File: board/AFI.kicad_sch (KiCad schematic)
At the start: 2 parts, among them J3 2002411212

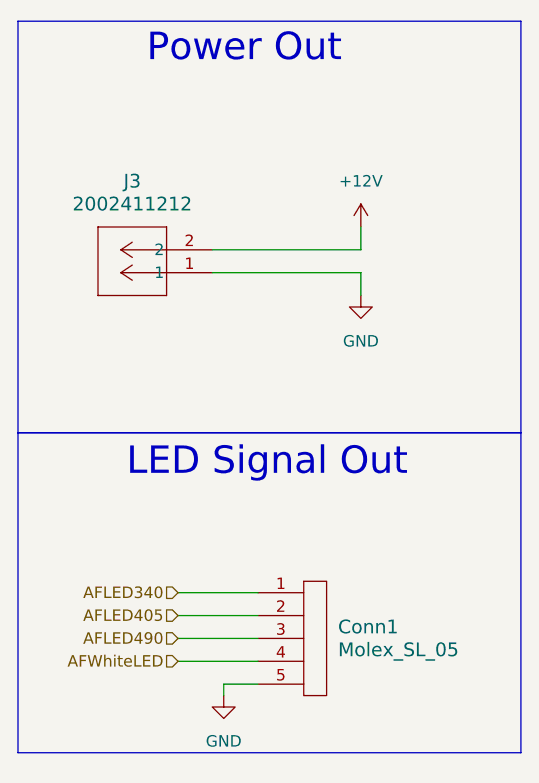
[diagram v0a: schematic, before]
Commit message: Swapped Pins for AF
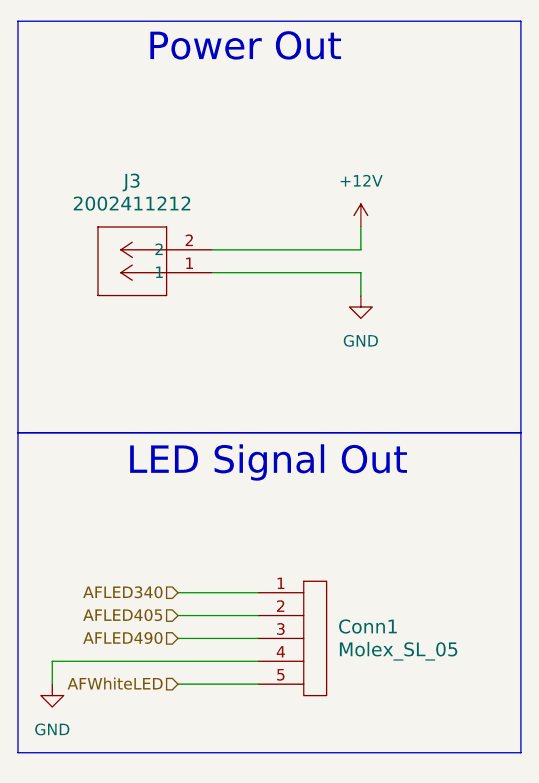
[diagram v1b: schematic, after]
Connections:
- net AFWhiteLED: now also Conn1.5; no longer Conn1.4
- net GND: now also Conn1.4; no longer Conn1.5
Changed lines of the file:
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@@
-	(wire
-		(pts
-			(xy 35.56 86.36) (xy 39.37 86.36)
-		)
-		(stroke
-			(width 0)
-			(type default)
-		)
-	)
 	(wire
 		(pts
@@
 	(wire
 		(pts
-			(xy 35.56 87.63) (xy 35.56 86.36)
+			(xy 16.51 83.82) (xy 39.37 83.82)
 		)
 		(stroke
@@
 	(wire
 		(pts
-			(xy 30.48 83.82) (xy 39.37 83.82)
+			(xy 30.48 86.36) (xy 39.37 86.36)
+		)
+		(stroke
+			(width 0)
+			(type default)
+		)
+	)
+	(wire
+		(pts
+			(xy 16.51 83.82) (xy 16.51 86.36)
 		)
 		(stroke
@@
 	(hierarchical_label "AFWhiteLED"
 		(shape input)
-		(at 30.48 83.82 180)
+		(at 30.48 86.36 180)
 		(effects
 			(font
@@
 	(symbol
 		(lib_id "power:GND")
-		(at 35.56 87.63 0)
+		(at 16.51 86.36 0)
 		(unit 1)
 		(exclude_from_sim no)
@@
 		(fields_autoplaced yes)
 		(property "Reference" "#PWR057"
-			(at 35.56 93.98 0)
+			(at 16.51 92.71 0)
 			(effects
 				(font
@@
 		)
 		(property "Value" "GND"
-			(at 35.56 92.71 0)
+			(at 16.51 91.44 0)
 			(effects
 				(font
@@
 		)
 		(property "Footprint" ""
-			(at 35.56 87.63 0)
+			(at 16.51 86.36 0)
 			(effects
 				(font
@@
 		)
 		(property "Datasheet" ""
-			(at 35.56 87.63 0)
+			(at 16.51 86.36 0)
 			(effects
 				(font
@@
 		)
 		(property "Description" "Power symbol creates a global label with name \"GND\" , ground"
-			(at 35.56 87.63 0)
-			(effects
-				(font
+			(at 16.51 86.36 0)
+			(effects
+				(font

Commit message: Repin AF Board Connector
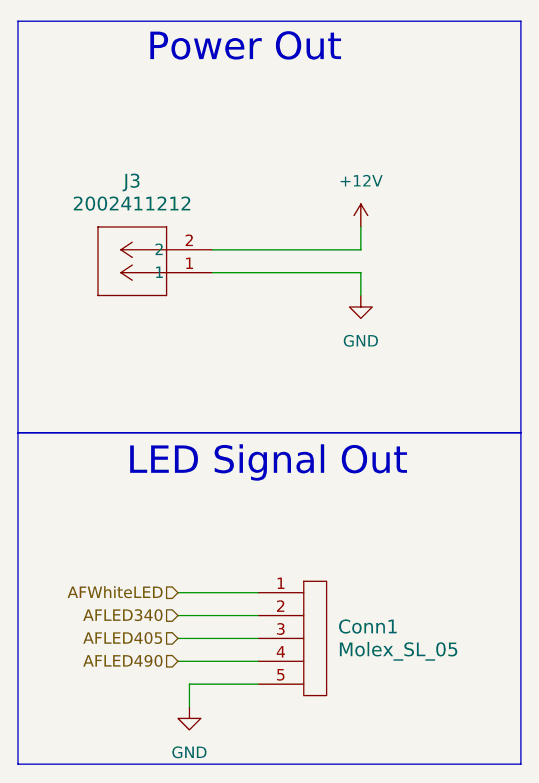
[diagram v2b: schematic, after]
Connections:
- net AFLED340: now also Conn1.2; no longer Conn1.1
- net AFLED405: now also Conn1.3; no longer Conn1.2
- net AFLED490: now also Conn1.4; no longer Conn1.3
- net AFWhiteLED: now also Conn1.1; no longer Conn1.5
- net GND: now also Conn1.5; no longer Conn1.4
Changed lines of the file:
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@@
 	(rectangle
 		(start 12.7 58.42)
-		(end 68.58 93.98)
+		(end 68.58 95.25)
 		(stroke
 			(width 0)
@@
 	(wire
 		(pts
+			(xy 50.8 40.64) (xy 34.29 40.64)
+		)
+		(stroke
+			(width 0)
+			(type default)
+		)
+	)
+	(wire
+		(pts
+			(xy 31.75 86.36) (xy 39.37 86.36)
+		)
+		(stroke
+			(width 0)
+			(type default)
+		)
+	)
+	(wire
+		(pts
 			(xy 30.48 81.28) (xy 39.37 81.28)
 		)
@@
 	(wire
 		(pts
-			(xy 50.8 40.64) (xy 34.29 40.64)
-		)
-		(stroke
-			(width 0)
-			(type default)
-		)
-	)
-	(wire
-		(pts
-			(xy 16.51 83.82) (xy 39.37 83.82)
-		)
-		(stroke
-			(width 0)
-			(type default)
-		)
-	)
-	(wire
-		(pts
 			(xy 50.8 35.56) (xy 50.8 38.1)
 		)
@@
 	(wire
 		(pts
+			(xy 30.48 76.2) (xy 39.37 76.2)
+		)
+		(stroke
+			(width 0)
+			(type default)
+		)
+	)
+	(wire
+		(pts
 			(xy 50.8 38.1) (xy 34.29 38.1)
 		)
@@
 	(wire
 		(pts
-			(xy 30.48 86.36) (xy 39.37 86.36)
-		)
-		(stroke
-			(width 0)
-			(type default)
-		)
-	)
-	(wire
-		(pts
-			(xy 16.51 83.82) (xy 16.51 86.36)
-		)
-		(stroke
-			(width 0)
-			(type default)
-		)
-	)
-	(wire
-		(pts
-			(xy 30.48 76.2) (xy 39.37 76.2)
+			(xy 31.75 86.36) (xy 31.75 88.9)
+		)
+		(stroke
+			(width 0)
+			(type default)
+		)
+	)
+	(wire
+		(pts
+			(xy 30.48 83.82) (xy 39.37 83.82)
 		)
 		(stroke
@@
 	(hierarchical_label "AFWhiteLED"
 		(shape input)
-		(at 30.48 86.36 180)
+		(at 30.48 76.2 180)
 		(effects
 			(font
@@
 	(hierarchical_label "AFLED405"
 		(shape input)
-		(at 30.48 78.74 180)
+		(at 30.48 81.28 180)
 		(effects
 			(font
@@
 	(hierarchical_label "AFLED490"
 		(shape input)
-		(at 30.48 81.28 180)
+		(at 30.48 83.82 180)
 		(effects
 			(font
@@
 	(hierarchical_label "AFLED340"
 		(shape input)
-		(at 30.48 76.2 180)
+		(at 30.48 78.74 180)
 		(effects
 			(font
@@
 	(symbol
 		(lib_id "power:GND")
-		(at 16.51 86.36 0)
+		(at 31.75 88.9 0)
 		(unit 1)
 		(exclude_from_sim no)
@@
 		(fields_autoplaced yes)
 		(property "Reference" "#PWR057"
-			(at 16.51 92.71 0)
+			(at 31.75 95.25 0)
 			(effects
 				(font
@@
 		)
 		(property "Value" "GND"
-			(at 16.51 91.44 0)
+			(at 31.75 93.98 0)
 			(effects
 				(font
@@
 		)
 		(property "Footprint" ""
-			(at 16.51 86.36 0)
+			(at 31.75 88.9 0)
 			(effects
 				(font
@@
 		)
 		(property "Datasheet" ""
-			(at 16.51 86.36 0)
+			(at 31.75 88.9 0)
 			(effects
 				(font
@@
 		)
 		(property "Description" "Power symbol creates a global label with name \"GND\" , ground"
-			(at 16.51 86.36 0)
-			(effects
-				(font
+			(at 31.75 88.9 0)
+			(effects
+				(font

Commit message: Caught mislabeled pinout for AF after the recent pin change
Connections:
- net AFLED340 renamed AFLED365
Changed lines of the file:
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@@
 		)
 	)
-	(hierarchical_label "AFLED340"
+	(hierarchical_label "AFLED365"
 		(shape input)
 		(at 30.48 78.74 180)
